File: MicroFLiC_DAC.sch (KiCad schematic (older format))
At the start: 33 parts, among them P1 8-way Micro-MaTch, P2 2x4 header strip, P3 1x2 header strip, P4 1x2 socket strip, P5 SMA, P6 SMA, P7 SMA, P8 SMA, U1 DAC8734

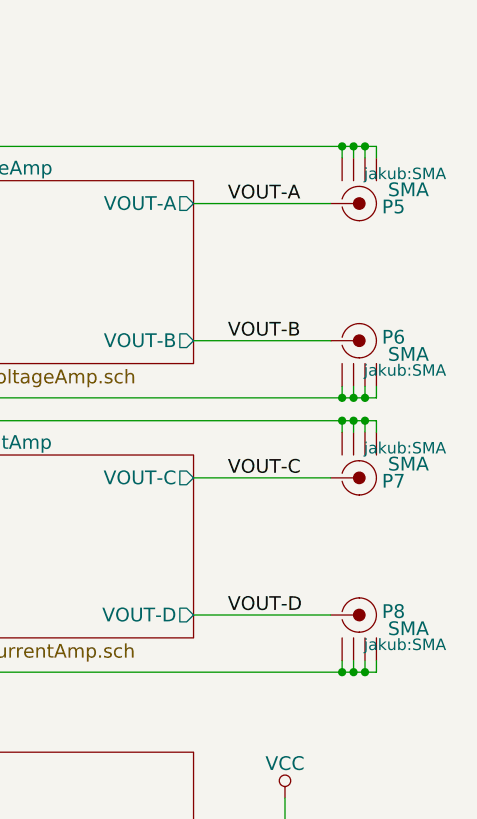
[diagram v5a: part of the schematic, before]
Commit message: Fixed SMA connector labels and 4u7/25V capacitor order code
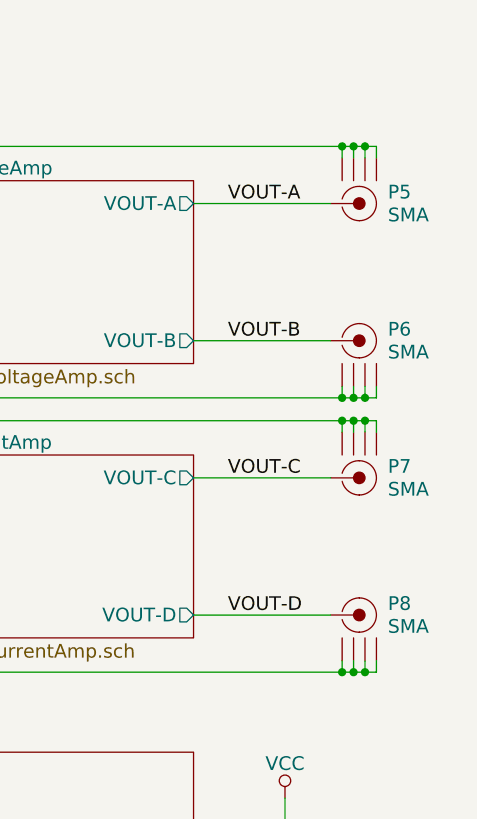
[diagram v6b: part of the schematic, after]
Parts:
- P5, P6, P7, P8: Note R/A SMA jack -> Right-angle SMA jack
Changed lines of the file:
@@
 U 1 1 557355CB
 P 10650 1250
-F 0 "P5" H 10775 1565 60  0000 C CNN
-F 1 "SMA" H 10840 1490 60  0000 C CNN
-F 2 "jakub:SMA" H 10825 1420 50  0000 C CNN
+F 0 "P5" H 10750 1500 60  0000 L CNN
+F 1 "SMA" H 10750 1600 60  0000 L CNN
+F 2 "jakub:SMA" H 10825 1420 50  0001 C CNN
 F 3 "" H 10650 1250 60  0000 C CNN
 F 4 "73251-2200" H 10650 1250 60  0001 C CNN "Part Number"
@@
 F 9 "Mouser" H 10650 1250 60  0001 C CNN "Alt. Supplier"
 F 10 "538-73251-2200" H 10650 1250 60  0001 C CNN "Alt. Order Code"
-F 11 "R/A SMA jack" H 10650 1250 60  0001 C CNN "Note"
+F 11 "Right-angle SMA jack" H 10650 1250 60  0001 C CNN "Note"
 	1    10650 1250
 	1    0    0    1
@@
 U 1 1 5573563A
 P 10650 2450
-F 0 "P6" H 10775 2765 60  0000 C CNN
-F 1 "SMA" H 10840 2690 60  0000 C CNN
-F 2 "jakub:SMA" H 10825 2620 50  0000 C CNN
+F 0 "P6" H 10750 2800 60  0000 L CNN
+F 1 "SMA" H 10750 2700 60  0000 L CNN
+F 2 "jakub:SMA" H 10825 2620 50  0001 C CNN
 F 3 "" H 10650 2450 60  0000 C CNN
 F 4 "73251-2200" H 10650 1250 60  0001 C CNN "Part Number"
@@
 F 9 "Mouser" H 10650 2450 60  0001 C CNN "Alt. Supplier"
 F 10 "538-73251-2200" H 10650 2450 60  0001 C CNN "Alt. Order Code"
-F 11 "R/A SMA jack" H 10650 2450 60  0001 C CNN "Note"
+F 11 "Right-angle SMA jack" H 10650 2450 60  0001 C CNN "Note"
 	1    10650 2450
 	1    0    0    -1
@@
 U 1 1 5573712F
 P 10650 2450
-F 0 "P7" H 10775 2765 60  0000 C CNN
-F 1 "SMA" H 10840 2690 60  0000 C CNN
-F 2 "jakub:SMA" H 10825 2620 50  0000 C CNN
+F 0 "P7" H 10750 2700 60  0000 L CNN
+F 1 "SMA" H 10750 2800 60  0000 L CNN
+F 2 "jakub:SMA" H 10825 2620 50  0001 C CNN
 F 3 "" H 10650 2450 60  0000 C CNN
 F 4 "73251-2200" H 10650 1250 60  0001 C CNN "Part Number"
@@
 F 9 "Mouser" H 10650 2450 60  0001 C CNN "Alt. Supplier"
 F 10 "538-73251-2200" H 10650 2450 60  0001 C CNN "Alt. Order Code"
-F 11 "R/A SMA jack" H 10650 2450 60  0001 C CNN "Note"
+F 11 "Right-angle SMA jack" H 10650 2450 60  0001 C CNN "Note"
 	1    10650 2450
 	1    0    0    1
@@
 U 1 1 55737135
 P 10650 3650
-F 0 "P8" H 10775 3965 60  0000 C CNN
-F 1 "SMA" H 10840 3890 60  0000 C CNN
-F 2 "jakub:SMA" H 10825 3820 50  0000 C CNN
+F 0 "P8" H 10750 4000 60  0000 L CNN
+F 1 "SMA" H 10750 3900 60  0000 L CNN
+F 2 "jakub:SMA" H 10825 3820 50  0001 C CNN
 F 3 "" H 10650 3650 60  0000 C CNN
 F 4 "73251-2200" H 10650 1250 60  0001 C CNN "Part Number"
@@
 F 9 "Mouser" H 10650 3650 60  0001 C CNN "Alt. Supplier"
 F 10 "538-73251-2200" H 10650 3650 60  0001 C CNN "Alt. Order Code"
-F 11 "R/A SMA jack" H 10650 3650 60  0001 C CNN "Note"
+F 11 "Right-angle SMA jack" H 10650 3650 60  0001 C CNN "Note"
 	1    10650 3650
 	1    0    0    -1

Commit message: Expanded the board for better grounding. OP-AMPs close to connectors
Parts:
- A1: footprint jakub:JMP -> jakub:solder_jumper
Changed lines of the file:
@@
 F 0 "A1" H 8100 6150 60  0000 C CNN
 F 1 "JMP" H 8100 5850 60  0000 C CNN
-F 2 "jakub:JMP" H 8100 6000 60  0001 C CNN
+F 2 "jakub:solder_jumper" H 8100 6000 60  0001 C CNN
 F 3 "" H 8100 6000 60  0000 C CNN
 	1    8100 6000

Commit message: Extended board
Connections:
- wire segments 196 -> 194
- no-connect marks 3 -> 5
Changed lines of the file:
@@
 $EndComp
 Wire Wire Line
-	9000 5900 8900 5900
-Wire Wire Line
-	8900 5900 8900 6100
+	8900 6000 8900 6100
 Wire Wire Line
 	8900 6000 9000 6000
@@
 Wire Wire Line
 	8900 5350 8900 5550
-Wire Wire Line
-	8900 5450 9000 5450
-Connection ~ 8900 5450
 $Comp
 L GNDA #PWR030
@@
 NoConn ~ 5100 2050
 NoConn ~ 5100 2150
+NoConn ~ 9000 5900
+NoConn ~ 9000 5450
 $EndSCHEMATC
